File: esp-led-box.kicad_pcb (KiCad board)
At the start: 2 copper layers, 26 parts, among them J1 Conn_01x03, J2 Conn_01x02_Female, J3 Conn_01x03_Female, Q1 BSS138, U1 ESP-12F, U2 MP2307, U3 LM3940

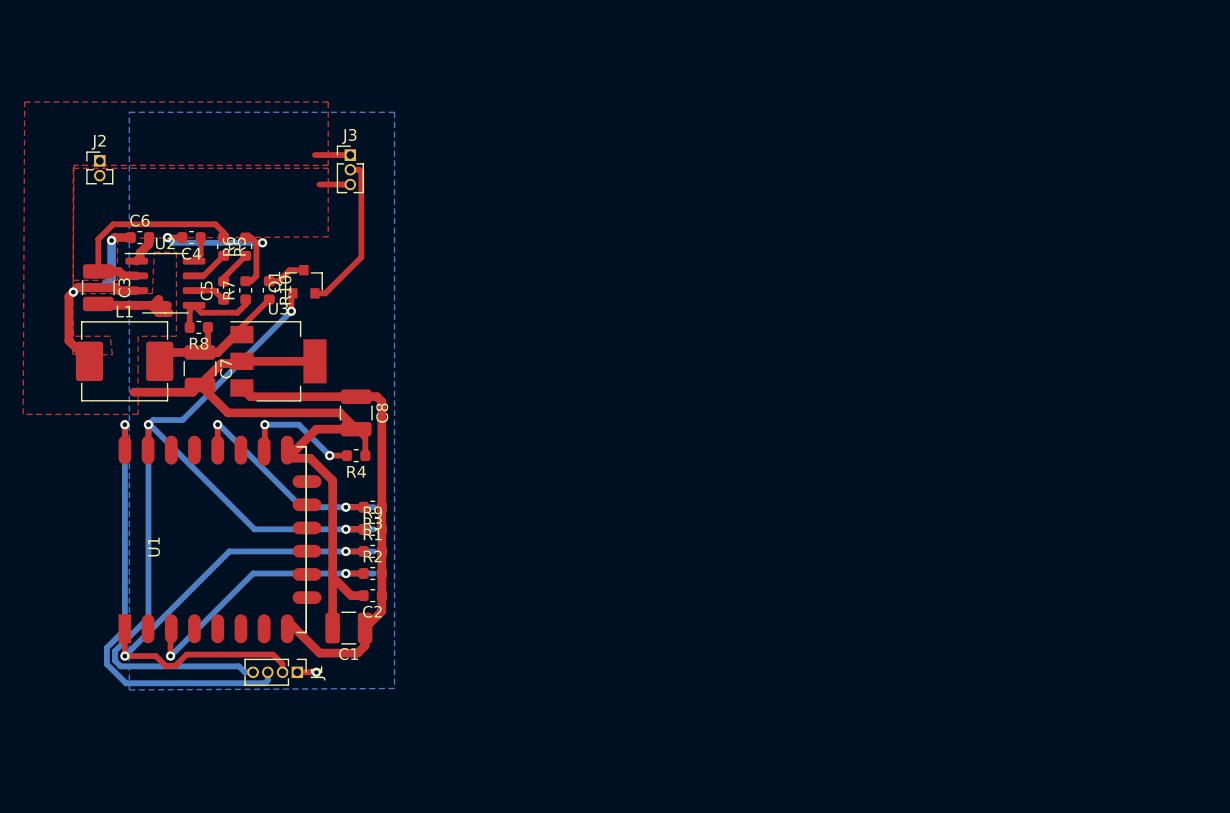
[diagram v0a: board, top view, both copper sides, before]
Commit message: Fixed iteration #2
- replace 0603 SMDs with 1206 ones;
- add fuse holder
- add two ACT LEDs
- fix level shifter transistor scheme
- add degson terminal block
- use 2.56 pin header
- add GPIO0, +3.3v pins to pin header
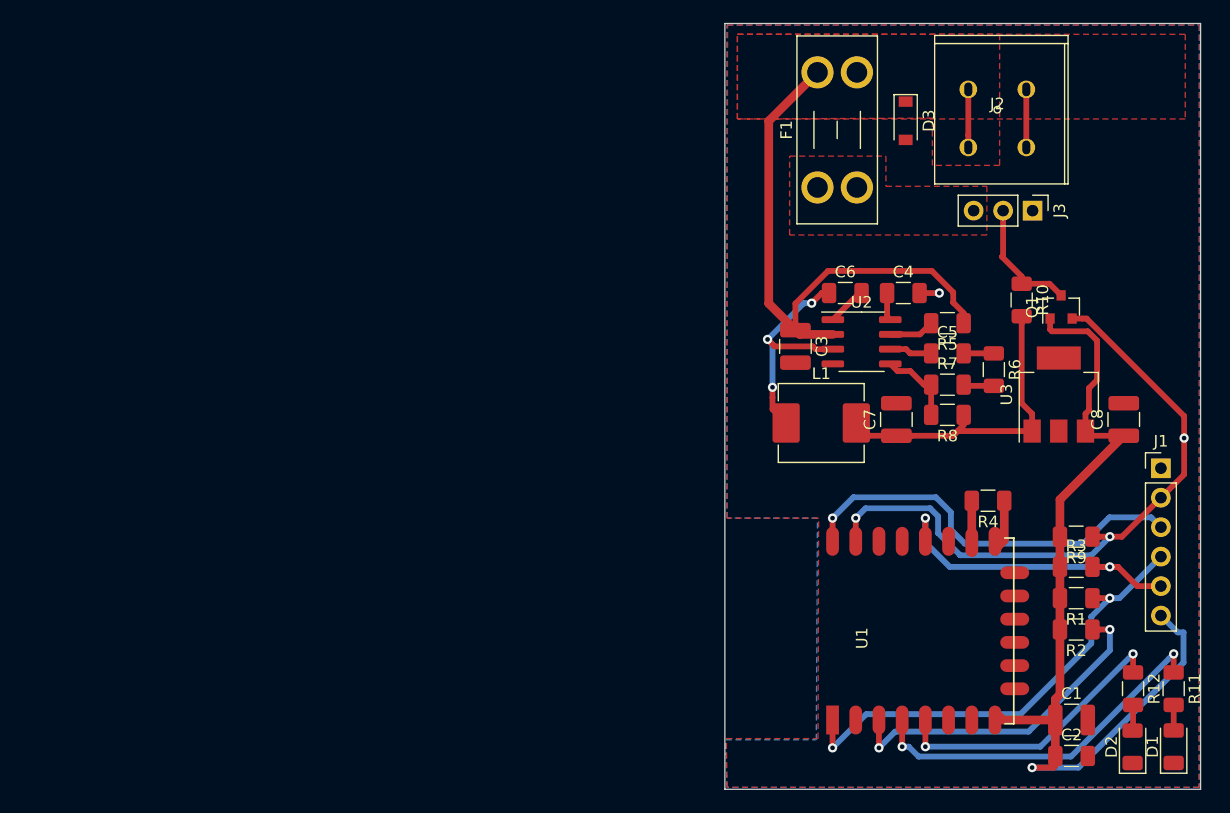
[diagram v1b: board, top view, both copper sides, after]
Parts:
- added D1: LED, LED_SMD:LED_1206_3216Metric, F.Cu at (149.7, 102.3)
- added D2: LED, LED_SMD:LED_1206_3216Metric, F.Cu at (146.2, 102.3)
- added D3: D, Diode_SMD:D_SOD-123, F.Cu at (126.6, 48.4)
- added F1: Fuse, Fuse:Fuseholder_Blade_Mini_Keystone_3568, F.Cu at (119.0, 54.1)
- added R11: 120, Resistor_SMD:R_1206_3216Metric, F.Cu at (149.7, 97.3)
- added R12: 120, Resistor_SMD:R_1206_3216Metric, F.Cu at (146.2, 97.3)
- C2, C4, C5, C6: footprint Capacitor_SMD:C_0603_1608Metric -> Capacitor_SMD:C_1206_3216Metric
- J1: footprint Connector_PinHeader_1.27mm:PinHeader_1x04_P1.27mm_Vertical -> Connector_PinHeader_2.54mm:PinHeader_1x06_P2.54mm_Vertical
- J2: footprint Connector_PinHeader_1.27mm:PinHeader_1x02_P1.27mm_Vertical -> esp-light-box:WG235-2P
- J3: footprint Connector_PinHeader_1.27mm:PinHeader_1x03_P1.27mm_Vertical -> Connector_PinHeader_2.54mm:PinHeader_1x03_P2.54mm_Vertical
- R1, R10, R2, R3, R4, R5, R6, R7, R8, R9: footprint Resistor_SMD:R_0603_1608Metric -> Resistor_SMD:R_1206_3216Metric
- moved J1 76.5 mm to (148.6, 78.3), turned to 0 degrees
- moved J2 72.0 mm to (129.1, 53.8), turned to 270 degrees
- moved U3 67.3 mm to (139.8, 72.0), turned to 90 degrees
- moved C8 66.2 mm to (145.4, 74.1), turned to 90 degrees
- moved R6 65.3 mm to (134.2, 69.8), turned to 270 degrees
- moved Q1 65.3 mm to (140.0, 64.4)
- moved R8 65.0 mm to (130.2, 73.7)
- moved R10 64.9 mm to (136.6, 63.8)
- moved C1 62.8 mm to (140.9, 100.0), turned to 0 degrees
- moved R5 62.7 mm to (130.2, 65.8), turned to 180 degrees
- moved C5 62.6 mm to (130.2, 68.4), turned to 0 degrees
- moved C2 61.8 mm to (140.9, 103.1), turned to 0 degrees
- moved C4 61.5 mm to (126.4, 63.2), turned to 0 degrees
- moved U1 61.5 mm to (120.3, 99.3)
- moved R7 61.0 mm to (130.2, 71.1), turned to 0 degrees
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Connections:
- J1 pad 2: /RESET -> /RXD|CONTROL
- J1 pad 4: /RXD|CONTROL -> /RESET
- J3 pad 3: +12V -> Net-(F1-Pad1)
- Q1 pad 1: /RXD|CONTROL -> +3V3
- Q1 pad 2: Net-(J3-Pad2) -> /RXD|CONTROL
- Q1 pad 3: Net-(Q1-Pad3) -> Net-(J3-Pad2)
- R10 pad 1: Net-(Q1-Pad3) -> Net-(J3-Pad2)
- R3 pad 2: Net-(R3-Pad2) -> GPIO0
- U1 pad 12: Net-(R3-Pad2) -> GPIO0
- U1 pad 4: Net-(U1-Pad4) -> GREEN_LED
- U1 pad 5: Net-(U1-Pad5) -> RED_LED
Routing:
- net GND: track 92.7 -> 13.9 mm, vias 3 -> 1
- net +3V3: track 43.2 -> 77.5 mm, vias 0 -> 1
- net +12V: track 21.0 -> 54.1 mm
- net GREEN_LED: track 0.00 -> 32.0 mm, vias 0 -> 2
- net GPIO0: track 0.00 -> 28.2 mm, vias 0 -> 2
- net RED_LED: track 0.00 -> 25.8 mm, vias 0 -> 2
- net /RXD|CONTROL: track 79.7 -> 56.4 mm
- net Net-(R3-Pad2): track 21.0 -> 0.00 mm, vias 2 -> 0
- net +5V: track 14.5 -> 29.6 mm
- net Net-(R4-Pad2): track 11.4 -> 4.20 mm, vias 2 -> 0
- net Net-(R2-Pad1): track 25.1 -> 29.8 mm
- net /TXD: track 39.8 -> 35.6 mm
- net /RESET: track 45.2 -> 41.1 mm
- net Net-(Q1-Pad3): track 3.38 -> 0.00 mm
- net Net-(J3-Pad2): track 13.7 -> 10.9 mm
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- added copper zone on F.Cu, net Net-(F1-Pad1)
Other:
- board outline added: 41 x 66 mm

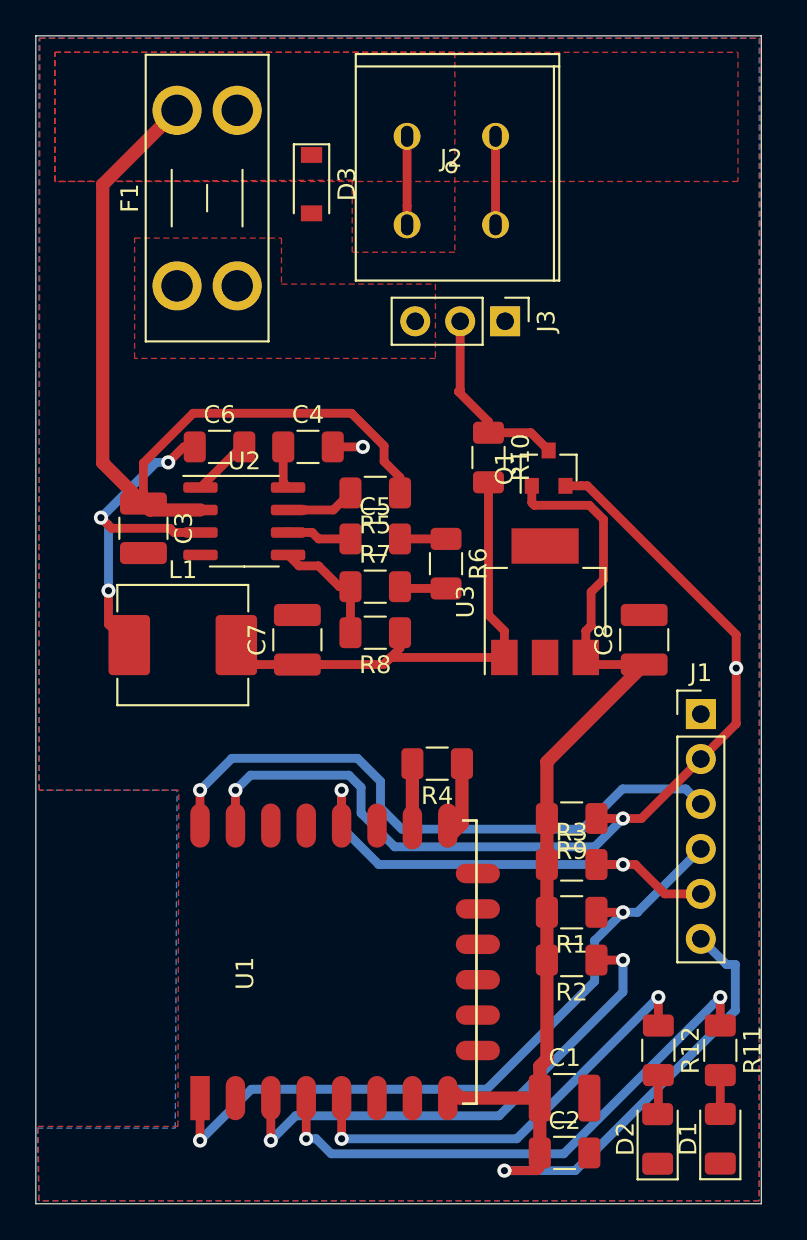
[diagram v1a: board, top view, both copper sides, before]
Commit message: pcb: make ready for manufacturing
- dummy resistors to switch from +12v power input to +5v input to make box be usable with different LED strips
- some cosmetic changes withing .sch
- put protection diode inline not parallel
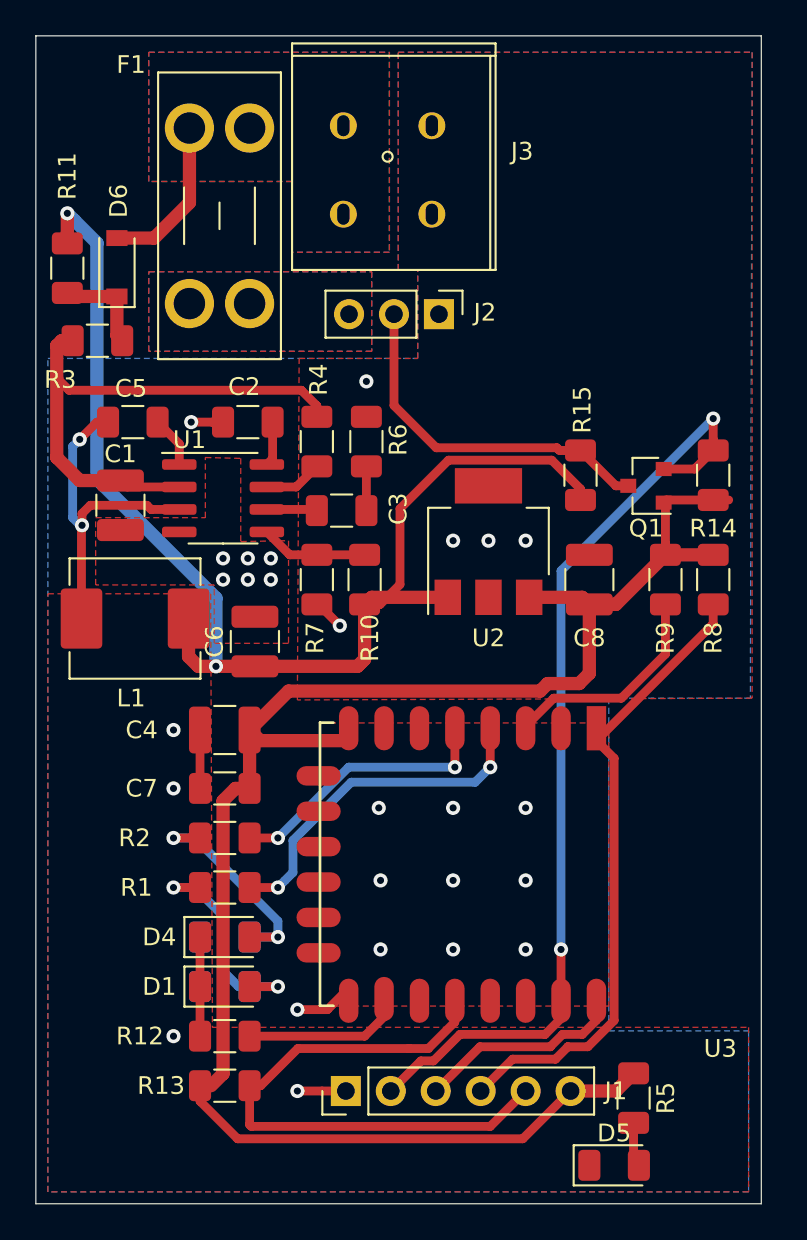
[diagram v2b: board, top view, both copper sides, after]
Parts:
- added D1: LED, LED_SMD:LED_1206_3216Metric, F.Cu at (121.7, 93.7)
- added D4: LED, LED_SMD:LED_1206_3216Metric, F.Cu at (121.7, 90.9)
- added D5: LED, LED_SMD:LED_1206_3216Metric, F.Cu at (143.7, 103.8)
- added R11: 0, Resistor_SMD:R_1206_3216Metric, F.Cu at (112.8, 53.1)
- added R3: 0, Resistor_SMD:R_1206_3216Metric, F.Cu at (114.5, 57.2)
- added R5: 120, Resistor_SMD:R_1206_3216Metric, F.Cu at (144.8, 100.0)
- D2: renamed from D1; moved to B.Cu
- D3: renamed from D2; moved to B.Cu
- moved U3 29.7 mm to (142.7, 79.8), turned to 270 degrees
- moved R1 29.5 mm to (121.7, 88.1), turned to 180 degrees
- moved D2 29.3 mm to (121.7, 93.7), turned to 0 degrees
- moved J1 29.3 mm to (128.5, 99.6), turned to 90 degrees
- moved C4 28.3 mm to (121.7, 79.2), turned to 180 degrees
- moved C7 28.2 mm to (121.7, 82.5), turned to 180 degrees
- moved R2 27.3 mm to (121.7, 85.3), turned to 180 degrees
- moved D3 27.0 mm to (121.7, 90.9), turned to 0 degrees
- moved R13 23.2 mm to (121.7, 99.3)
- moved R9 22.1 mm to (146.6, 70.7), turned to 90 degrees
- moved R14 21.0 mm to (149.3, 64.8), turned to 270 degrees
- moved R8 20.4 mm to (149.3, 70.7), turned to 90 degrees
- moved R12 19.5 mm to (121.7, 96.5), turned to 0 degrees
- moved D6 12.0 mm to (115.6, 53.0), turned to 90 degrees
- moved R6 8.24 mm to (129.7, 62.9), turned to 90 degrees
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- renumbered C3 to C1, C4 to C2, C5 to C3, C1 to C4, C6 to C5, C7 to C6, C2 to C7, D3 to D6, J3 to J2, J2 to J3, R11 to R1, R8 to R10, R4 to R12, R3 to R13, R9 to R14, R10 to R15, R12 to R2, R5 to R4, R1 to R8, R2 to R9, U2 to U1, U3 to U2, U1 to U3
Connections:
- net GPIO0 renamed /GPIO0
- net GREEN_LED renamed /GREEN_LED
- net RED_LED renamed /RED_LED
- C1 pad 1: +12V -> Net-(C1-Pad1)
- D6 pad 1: +12V -> +VDC
- D6 pad 2: GND -> VSS
- F1 pad 2: +12V -> VSS
- J3 pad 2: +12V -> VSS
- R4 pad 1: +12V -> Net-(C1-Pad1)
- U1 pad 2: +12V -> Net-(C1-Pad1)
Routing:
- net +12V: track 54.1 -> 0.00 mm
- net +5V: track 29.6 -> 70.6 mm, vias 0 -> 2
- net Net-(C1-Pad1): track 0.00 -> 30.9 mm
- net /TXD: track 35.6 -> 12.5 mm, vias 1 -> 0
- net +3V3: track 77.5 -> 99.2 mm, vias 1 -> 0
- net Net-(R9-Pad1): track 29.8 -> 13.2 mm, vias 2 -> 0
- net /GREEN_LED: track 32.0 -> 19.0 mm
- net Net-(D3-Pad2): track 2.23 -> 13.4 mm, vias 0 -> 2
- net /RED_LED: track 25.8 -> 14.8 mm
- net Net-(D1-Pad2): track 2.20 -> 13.2 mm, vias 0 -> 2
- net Net-(J2-Pad2): track 10.9 -> 21.2 mm
- net VSS: track 0.00 -> 9.15 mm
- net +VDC: track 0.00 -> 5.51 mm
- net /GPIO0: track 28.2 -> 33.7 mm, vias 2 -> 0
- net Net-(R12-Pad2): track 4.20 -> 9.66 mm
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- added copper zone on B.Cu, net Net-(F1-Pad1)
- added copper zone on B.Cu, net VSS
- added copper zone on F.Cu, net VSS
- removed copper zone on F.Cu, net +12V
